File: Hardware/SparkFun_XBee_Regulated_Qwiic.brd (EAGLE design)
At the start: 35.6 x 52.1 mm, 97 parts, among them J4 QWIIC_RIGHT_ANGLE, U2 AP63203

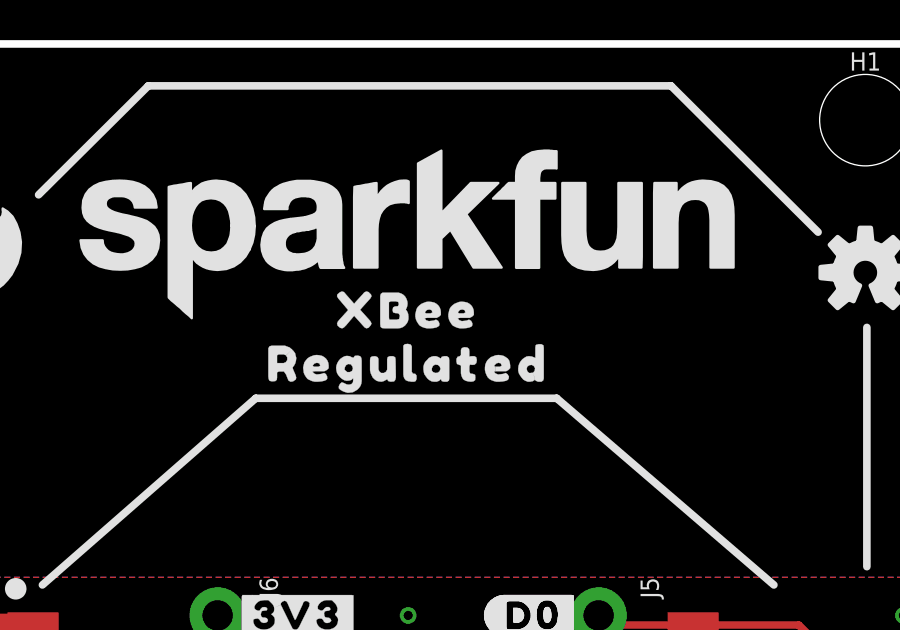
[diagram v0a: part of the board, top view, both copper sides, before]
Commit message: Adds "Explorer" to silk
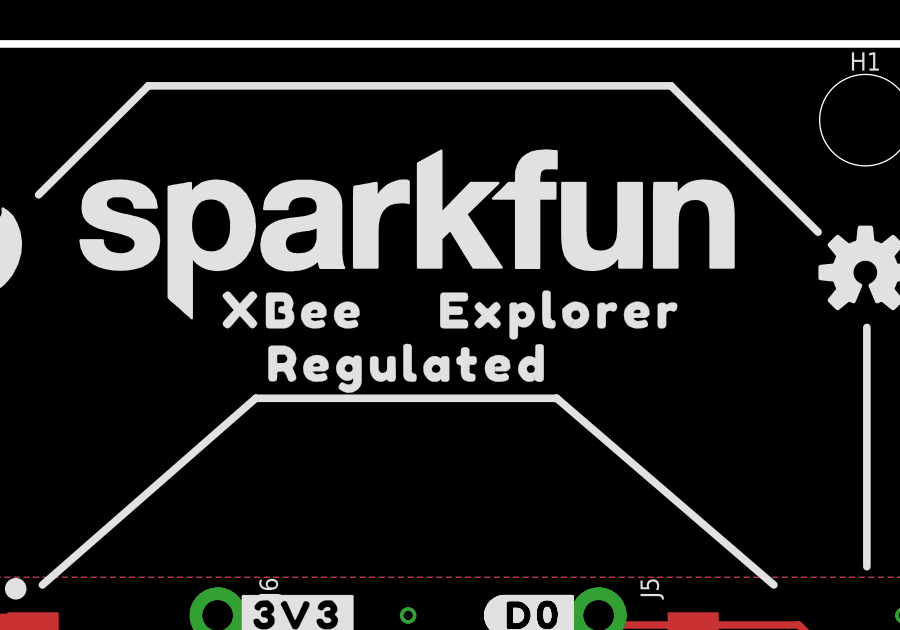
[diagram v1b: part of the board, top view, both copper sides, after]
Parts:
- added U$33: (no value), topmirror:EXPLORER1344
- U$23: device top:XBEE340 -> topmirror:EXPLORER1344
- moved U$23 5.08 mm to (11.4, 43.2)
- moved U$28 3.81 mm to (12.7, 43.2)
- moved U$25 3.81 mm to (20.3, 43.2)
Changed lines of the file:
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@@
 <layers>
 <layer number="1" name="Top" color="4" fill="1" visible="yes" active="yes"/>
-<layer number="2" name="Route2" color="23" fill="1" visible="yes" active="yes"/>
-<layer number="15" name="Route15" color="39" fill="1" visible="yes" active="yes"/>
+<layer number="2" name="Route2" color="23" fill="1" visible="no" active="yes"/>
+<layer number="15" name="Route15" color="39" fill="1" visible="no" active="yes"/>
 <layer number="16" name="Bottom" color="3" fill="1" visible="yes" active="yes"/>
 <layer number="17" name="Pads" color="26" fill="1" visible="yes" active="yes"/>
@@
 <element name="U$10" library="top" package="#D4#PICO#25" value="" x="18.542" y="10.16" smashed="yes" rot="MR0"/>
 <element name="U$24" library="topmirror" package="REGULATED1343" value="" x="16.51" y="41.402" smashed="yes" rot="MR0"/>
-<element name="U$25" library="top" package="XBEE340" value="" x="16.51" y="43.18" smashed="yes" rot="MR0"/>
-<element name="U$23" library="top" package="XBEE340" value="" x="16.51" y="43.18" smashed="yes" rot="MR0"/>
-<element name="U$28" library="top" package="XBEE340" value="" x="16.51" y="43.18" smashed="yes"/>
+<element name="U$25" library="top" package="XBEE340" value="" x="20.32" y="43.18" smashed="yes" rot="MR0"/>
+<element name="U$28" library="top" package="XBEE340" value="" x="12.7" y="43.18" smashed="yes"/>
 <element name="U$29" library="topmirror" package="REGULATED1343" value="" x="16.51" y="41.402" smashed="yes"/>
 <element name="U$31" library="botmirror" package="#D0#3" value="" x="20.701" y="33.02" smashed="yes"/>
@@
 <element name="LOGO4" library="SparkFun-Aesthetics" package="BLANK" value="SFE_LOGO_NAMEBLANK" x="-10.16" y="-27.94" smashed="yes"/>
 <element name="U$6" library="topmirror" package="#EN#17" value="" x="25.019" y="7.62" smashed="yes"/>
+<element name="U$33" library="topmirror" package="EXPLORER1344" value="" x="21.59" y="43.18" smashed="yes"/>
+<element name="U$23" library="topmirror" package="EXPLORER1344" value="" x="11.43" y="43.18" smashed="yes" rot="MR0"/>
 </elements>
 <signals>
